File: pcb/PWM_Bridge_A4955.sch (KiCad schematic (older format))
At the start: 18 parts, among them Q3 IPD220N06L3, Q4 IPD220N06L3, Q5 IPD220N06L3, Q6 IPD220N06L3, U5 A4955GLPTR-T

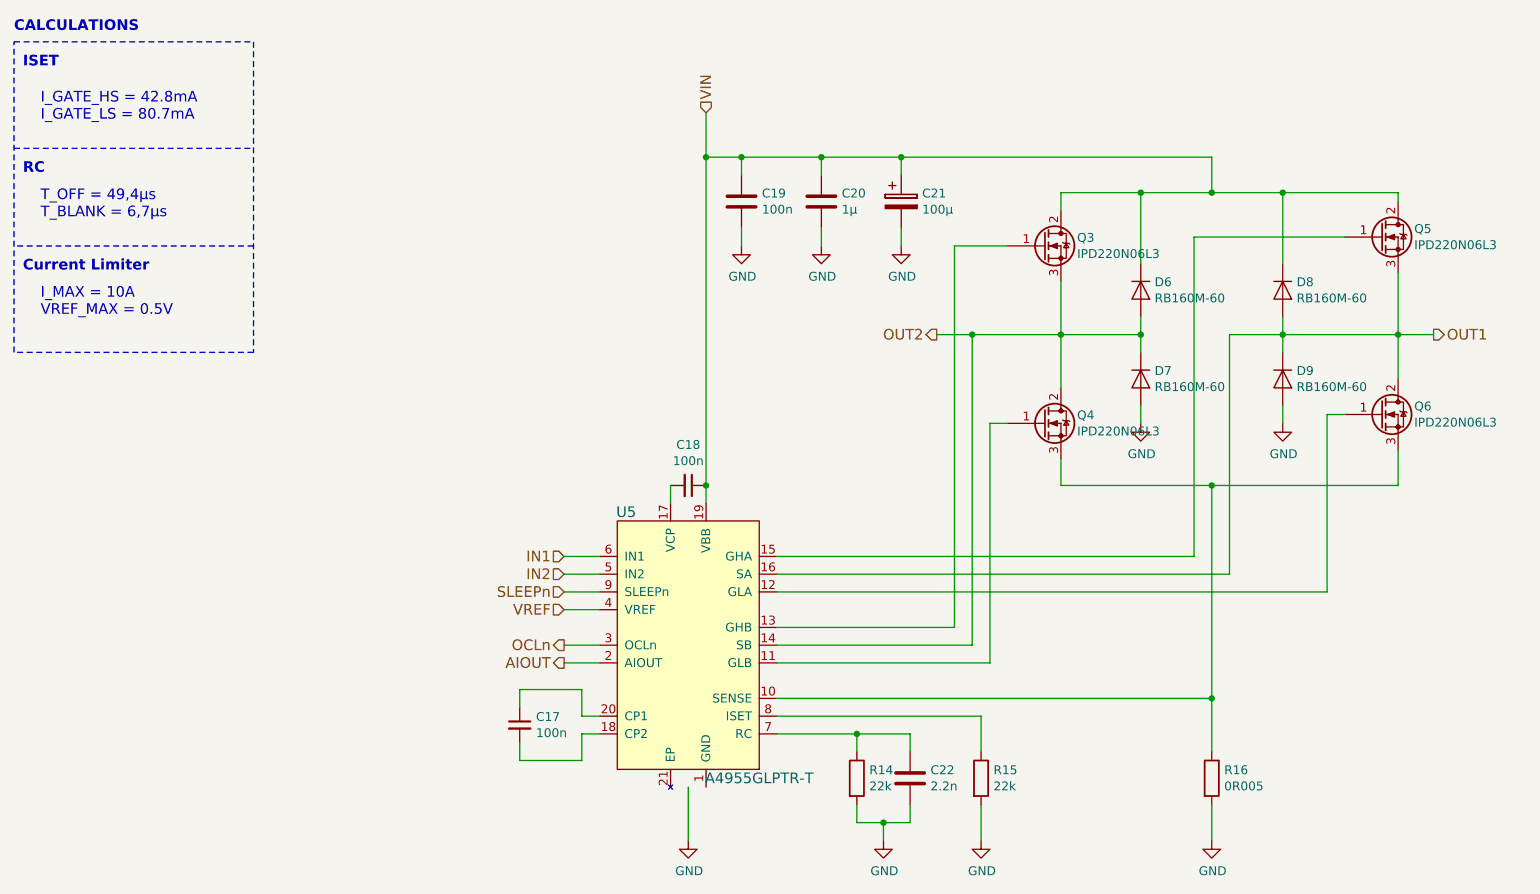
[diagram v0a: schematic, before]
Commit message: Use new library symbols
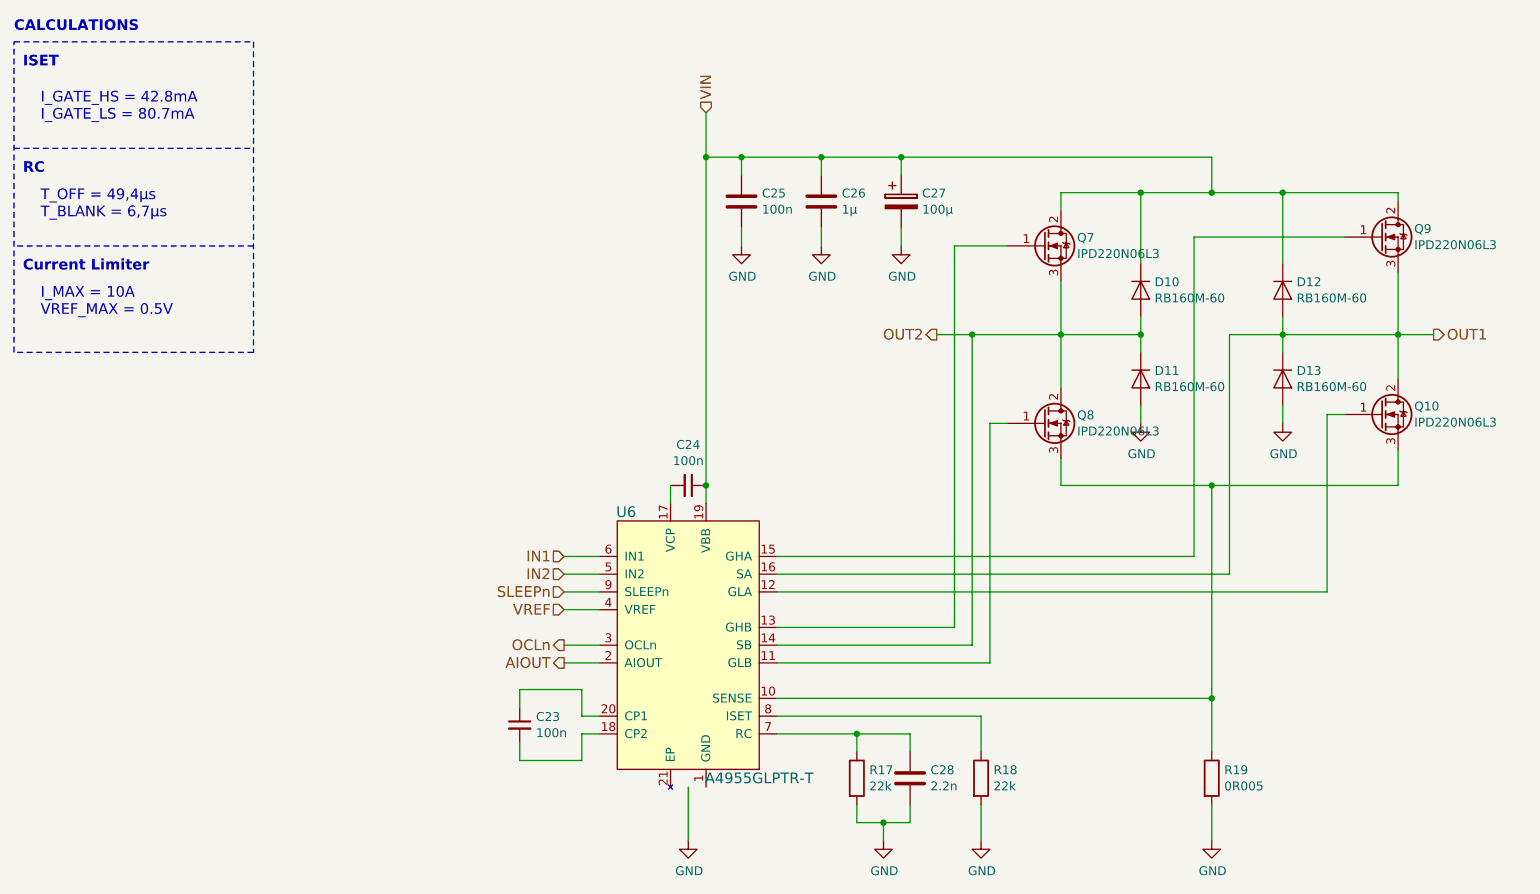
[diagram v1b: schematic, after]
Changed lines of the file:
@@
 $Descr A4 11693 8268
 encoding utf-8
-Sheet 3 7
+Sheet 4 7
 Title "A4955 PWM Bridge"
 Date "2016-10-22"
@@
 AR Path="/58077727/58077F1C" Ref="U5"  Part="1"
 AR Path="/58084D17/58077F1C" Ref="U6"  Part="1"
-F 0 "U5" H 4300 5150 60  0000 C CNN
+F 0 "U6" H 4300 5150 60  0000 C CNN
 F 1 "A4955GLPTR-T" H 5050 3650 60  0000 C CNN
 F 2 "Housings_SSOP:TSSOP-20_4.4x6.5mm_Pitch0.65mm" H 4650 4400 60  0001 C CNN
@@
 AR Path="/58077727/5807829A" Ref="C18"  Part="1"
 AR Path="/58084D17/5807829A" Ref="C24"  Part="1"
-F 0 "C18" V 4421 3500 50  0000 C CNN
+F 0 "C24" V 4421 3500 50  0000 C CNN
 F 1 "100n" V 4512 3500 50  0000 C CNN
 F 2 "Capacitors_SMD:C_0603" H 4650 3500 50  0001 C CNN
@@
 AR Path="/58077727/58078520" Ref="R14"  Part="1"
 AR Path="/58084D17/58078520" Ref="R17"  Part="1"
-F 0 "R14" H 5670 5196 50  0000 L CNN
+F 0 "R17" H 5670 5196 50  0000 L CNN
 F 1 "22k" H 5670 5105 50  0000 L CNN
 F 2 "Resistors_SMD:R_0603" V 5530 5150 50  0001 C CNN
@@
 AR Path="/58077727/5807867B" Ref="C22"  Part="1"
 AR Path="/58084D17/5807867B" Ref="C28"  Part="1"
-F 0 "C22" H 6015 5196 50  0000 L CNN
+F 0 "C28" H 6015 5196 50  0000 L CNN
 F 1 "2.2n" H 6015 5105 50  0000 L CNN
 F 2 "Capacitors_SMD:C_0603" H 5938 5000 50  0001 C CNN
@@
 AR Path="/58077727/580789CE" Ref="R16"  Part="1"
 AR Path="/58084D17/580789CE" Ref="R19"  Part="1"
-F 0 "R16" H 7670 5196 50  0000 L CNN
+F 0 "R19" H 7670 5196 50  0000 L CNN
 F 1 "0R005" H 7670 5105 50  0000 L CNN
 F 2 "Resistors_SMD:R_2512" V 7530 5150 50  0001 C CNN
@@
 AR Path="/58077727/58078C46" Ref="Q3"  Part="1"
 AR Path="/58084D17/58078C46" Ref="Q7"  Part="1"
-F 0 "Q3" H 6841 2196 50  0000 L CNN
+F 0 "Q7" H 6841 2196 50  0000 L CNN
 F 1 "IPD220N06L3" H 6841 2105 50  0000 L CNN
 F 2 "TO_SOT_Packages_SMD:TO-252-2Lead" H 6850 2250 50  0001 C CNN
@@
 AR Path="/58077727/58078E80" Ref="Q5"  Part="1"
 AR Path="/58084D17/58078E80" Ref="Q9"  Part="1"
-F 0 "Q5" H 8741 2146 50  0000 L CNN
+F 0 "Q9" H 8741 2146 50  0000 L CNN
 F 1 "IPD220N06L3" H 8741 2055 50  0000 L CNN
 F 2 "TO_SOT_Packages_SMD:TO-252-2Lead" H 8750 2200 50  0001 C CNN
@@
 AR Path="/58077727/58078ED9" Ref="Q6"  Part="1"
 AR Path="/58084D17/58078ED9" Ref="Q10"  Part="1"
-F 0 "Q6" H 8741 3146 50  0000 L CNN
+F 0 "Q10" H 8741 3146 50  0000 L CNN
 F 1 "IPD220N06L3" H 8741 3055 50  0000 L CNN
 F 2 "TO_SOT_Packages_SMD:TO-252-2Lead" H 8750 3200 50  0001 C CNN
@@
 AR Path="/58077727/58078F3F" Ref="Q4"  Part="1"
 AR Path="/58084D17/58078F3F" Ref="Q8"  Part="1"
-F 0 "Q4" H 6841 3196 50  0000 L CNN
+F 0 "Q8" H 6841 3196 50  0000 L CNN
 F 1 "IPD220N06L3" H 6841 3105 50  0000 L CNN
 F 2 "TO_SOT_Packages_SMD:TO-252-2Lead" H 6850 3250 50  0001 C CNN
@@
 AR Path="/58077727/5807A394" Ref="C19"  Part="1"
 AR Path="/58084D17/5807A394" Ref="C25"  Part="1"
-F 0 "C19" H 5065 1946 50  0000 L CNN
+F 0 "C25" H 5065 1946 50  0000 L CNN
 F 1 "100n" H 5065 1855 50  0000 L CNN
 F 2 "Capacitors_SMD:C_0603" H 4988 1750 50  0001 C CNN
@@
 AR Path="/58077727/5807A62E" Ref="C21"  Part="1"
 AR Path="/58084D17/5807A62E" Ref="C27"  Part="1"
-F 0 "C21" H 5968 1946 50  0000 L CNN
+F 0 "C27" H 5968 1946 50  0000 L CNN
 F 1 "100µ" H 5968 1855 50  0000 L CNN
 F 2 "Capacitors_SMD:c_elec_10x10" H 5888 1750 50  0001 C CNN
@@
 AR Path="/58077727/5807BEA4" Ref="C17"  Part="1"
 AR Path="/58084D17/5807BEA4" Ref="C23"  Part="1"
-F 0 "C17" H 3792 4896 50  0000 L CNN
+F 0 "C23" H 3792 4896 50  0000 L CNN
 F 1 "100n" H 3792 4805 50  0000 L CNN
 F 2 "Capacitors_SMD:C_0603" H 3700 4850 50  0001 C CNN
@@
 AR Path="/58077727/5809AC71" Ref="C20"  Part="1"
 AR Path="/58084D17/5809AC71" Ref="C26"  Part="1"
-F 0 "C20" H 5515 1946 50  0000 L CNN
+F 0 "C26" H 5515 1946 50  0000 L CNN
 F 1 "1µ" H 5515 1855 50  0000 L CNN
 F 2 "Capacitors_SMD:C_0603" H 5438 1750 50  0001 C CNN
@@
 AR Path="/58077727/580A461C" Ref="R15"  Part="1"
 AR Path="/58084D17/580A461C" Ref="R18"  Part="1"
-F 0 "R15" H 6370 5196 50  0000 L CNN
+F 0 "R18" H 6370 5196 50  0000 L CNN
 F 1 "22k" H 6370 5105 50  0000 L CNN
 F 2 "Resistors_SMD:R_0603" V 6230 5150 50  0001 C CNN
@@
 AR Path="/58077727/58151ECD" Ref="D6"  Part="1"
 AR Path="/58084D17/58151ECD" Ref="D10"  Part="1"
-F 0 "D6" V 7154 2478 50  0000 L CNN
+F 0 "D10" V 7154 2478 50  0000 L CNN
 F 1 "RB160M-60" V 7245 2478 50  0000 L CNN
 F 2 "Diodes_SMD:SOD-123" V 7291 2478 50  0001 L CNN
@@
 AR Path="/58077727/581537FD" Ref="D7"  Part="1"
 AR Path="/58084D17/581537FD" Ref="D11"  Part="1"
-F 0 "D7" V 7154 2978 50  0000 L CNN
+F 0 "D11" V 7154 2978 50  0000 L CNN
 F 1 "RB160M-60" V 7245 2978 50  0000 L CNN
 F 2 "Diodes_SMD:SOD-123" V 7291 2978 50  0001 L CNN
@@
 AR Path="/58077727/58153EBB" Ref="D9"  Part="1"
 AR Path="/58084D17/58153EBB" Ref="D13"  Part="1"
-F 0 "D9" V 7954 2978 50  0000 L CNN
+F 0 "D13" V 7954 2978 50  0000 L CNN
 F 1 "RB160M-60" V 8045 2978 50  0000 L CNN
 F 2 "Diodes_SMD:SOD-123" V 8091 2978 50  0001 L CNN
@@
 AR Path="/58077727/58153F12" Ref="D8"  Part="1"
 AR Path="/58084D17/58153F12" Ref="D12"  Part="1"
-F 0 "D8" V 7954 2478 50  0000 L CNN
+F 0 "D12" V 7954 2478 50  0000 L CNN
 F 1 "RB160M-60" V 8045 2478 50  0000 L CNN
 F 2 "Diodes_SMD:SOD-123" V 8091 2478 50  0001 L CNN

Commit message: Improve pcb routing
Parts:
- U5: footprint Housings_SSOP:TSSOP-20_4.4x6.5mm_Pitch0.65mm -> Housings_SSOP:ETSSOP-20-1EP_4.4x6.5mm_Pitch0.65mm
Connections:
- net GND: now also U5.1 (GND), U5.21 (EP)
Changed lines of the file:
@@
 $Descr A4 11693 8268
 encoding utf-8
-Sheet 4 7
+Sheet 3 7
 Title "A4955 PWM Bridge"
 Date "2016-10-22"
@@
 AR Path="/58077727/58077F1C" Ref="U5"  Part="1"
 AR Path="/58084D17/58077F1C" Ref="U6"  Part="1"
-F 0 "U6" H 4300 5150 60  0000 C CNN
-F 1 "A4955GLPTR-T" H 5050 3650 60  0000 C CNN
-F 2 "Housings_SSOP:TSSOP-20_4.4x6.5mm_Pitch0.65mm" H 4650 4400 60  0001 C CNN
+F 0 "U5" H 4300 5150 60  0000 C CNN
+F 1 "A4955GLPTR-T" H 5100 3650 60  0000 C CNN
+F 2 "Housings_SSOP:ETSSOP-20-1EP_4.4x6.5mm_Pitch0.65mm" H 4650 4400 60  0001 C CNN
 F 3 "http://www.allegromicro.com/~/media/Files/Datasheets/A4955-Datasheet.ashx?la=en" H 4650 4400 60  0001 C CNN
 F 4 "620-1770-1-ND" H 4650 4400 60  0001 C CNN "Digi-Key Part Number"
@@
 AR Path="/58077727/5807829A" Ref="C18"  Part="1"
 AR Path="/58084D17/5807829A" Ref="C24"  Part="1"
-F 0 "C24" V 4421 3500 50  0000 C CNN
+F 0 "C18" V 4421 3500 50  0000 C CNN
 F 1 "100n" V 4512 3500 50  0000 C CNN
 F 2 "Capacitors_SMD:C_0603" H 4650 3500 50  0001 C CNN
@@
 AR Path="/58077727/58078520" Ref="R14"  Part="1"
 AR Path="/58084D17/58078520" Ref="R17"  Part="1"
-F 0 "R17" H 5670 5196 50  0000 L CNN
+F 0 "R14" H 5670 5196 50  0000 L CNN
 F 1 "22k" H 5670 5105 50  0000 L CNN
 F 2 "Resistors_SMD:R_0603" V 5530 5150 50  0001 C CNN
@@
 AR Path="/58077727/5807867B" Ref="C22"  Part="1"
 AR Path="/58084D17/5807867B" Ref="C28"  Part="1"
-F 0 "C28" H 6015 5196 50  0000 L CNN
+F 0 "C22" H 6015 5196 50  0000 L CNN
 F 1 "2.2n" H 6015 5105 50  0000 L CNN
 F 2 "Capacitors_SMD:C_0603" H 5938 5000 50  0001 C CNN
@@
 AR Path="/58077727/580787DB" Ref="#PWR063"  Part="1"
 AR Path="/58084D17/580787DB" Ref="#PWR072"  Part="1"
-F 0 "#PWR072" H 5750 5250 50  0001 C CNN
+F 0 "#PWR063" H 5750 5250 50  0001 C CNN
 F 1 "GND" H 5755 5327 50  0000 C CNN
 F 2 "" H 5750 5500 50  0000 C CNN
@@
 L GND #PWR064
 U 1 1 58078835
-P 4650 5500
+P 4750 5500
 AR Path="/58077727/58078835" Ref="#PWR064"  Part="1"
 AR Path="/58084D17/58078835" Ref="#PWR073"  Part="1"
-F 0 "#PWR073" H 4650 5250 50  0001 C CNN
-F 1 "GND" H 4655 5327 50  0000 C CNN
-F 2 "" H 4650 5500 50  0000 C CNN
-F 3 "" H 4650 5500 50  0000 C CNN
-	1    4650 5500
+F 0 "#PWR064" H 4750 5250 50  0001 C CNN
+F 1 "GND" H 4755 5327 50  0000 C CNN
+F 2 "" H 4750 5500 50  0000 C CNN
+F 3 "" H 4750 5500 50  0000 C CNN
+	1    4750 5500
 	1    0    0    -1
 $EndComp
@@
 AR Path="/58077727/580789CE" Ref="R16"  Part="1"
 AR Path="/58084D17/580789CE" Ref="R19"  Part="1"
-F 0 "R19" H 7670 5196 50  0000 L CNN
+F 0 "R16" H 7670 5196 50  0000 L CNN
 F 1 "0R005" H 7670 5105 50  0000 L CNN
 F 2 "Resistors_SMD:R_2512" V 7530 5150 50  0001 C CNN
@@
 AR Path="/58077727/58078AB1" Ref="#PWR065"  Part="1"
 AR Path="/58084D17/58078AB1" Ref="#PWR074"  Part="1"
-F 0 "#PWR074" H 7600 5250 50  0001 C CNN
+F 0 "#PWR065" H 7600 5250 50  0001 C CNN
 F 1 "GND" H 7605 5327 50  0000 C CNN
 F 2 "" H 7600 5500 50  0000 C CNN
@@
 AR Path="/58077727/58078C46" Ref="Q3"  Part="1"
 AR Path="/58084D17/58078C46" Ref="Q7"  Part="1"
-F 0 "Q7" H 6841 2196 50  0000 L CNN
+F 0 "Q3" H 6841 2196 50  0000 L CNN
 F 1 "IPD220N06L3" H 6841 2105 50  0000 L CNN
 F 2 "TO_SOT_Packages_SMD:TO-252-2Lead" H 6850 2250 50  0001 C CNN
@@
 AR Path="/58077727/58078E80" Ref="Q5"  Part="1"
 AR Path="/58084D17/58078E80" Ref="Q9"  Part="1"
-F 0 "Q9" H 8741 2146 50  0000 L CNN
+F 0 "Q5" H 8741 2146 50  0000 L CNN
 F 1 "IPD220N06L3" H 8741 2055 50  0000 L CNN
 F 2 "TO_SOT_Packages_SMD:TO-252-2Lead" H 8750 2200 50  0001 C CNN
@@
 AR Path="/58077727/58078ED9" Ref="Q6"  Part="1"
 AR Path="/58084D17/58078ED9" Ref="Q10"  Part="1"
-F 0 "Q10" H 8741 3146 50  0000 L CNN
+F 0 "Q6" H 8741 3146 50  0000 L CNN
 F 1 "IPD220N06L3" H 8741 3055 50  0000 L CNN
 F 2 "TO_SOT_Packages_SMD:TO-252-2Lead" H 8750 3200 50  0001 C CNN
@@
 AR Path="/58077727/58078F3F" Ref="Q4"  Part="1"
 AR Path="/58084D17/58078F3F" Ref="Q8"  Part="1"
-F 0 "Q8" H 6841 3196 50  0000 L CNN
+F 0 "Q4" H 6841 3196 50  0000 L CNN
 F 1 "IPD220N06L3" H 6841 3105 50  0000 L CNN
 F 2 "TO_SOT_Packages_SMD:TO-252-2Lead" H 6850 3250 50  0001 C CNN
@@
 AR Path="/58077727/5807A394" Ref="C19"  Part="1"
 AR Path="/58084D17/5807A394" Ref="C25"  Part="1"
-F 0 "C25" H 5065 1946 50  0000 L CNN
+F 0 "C19" H 5065 1946 50  0000 L CNN
 F 1 "100n" H 5065 1855 50  0000 L CNN
 F 2 "Capacitors_SMD:C_0603" H 4988 1750 50  0001 C CNN
@@
 AR Path="/58077727/5807A4C6" Ref="#PWR066"  Part="1"
 AR Path="/58084D17/5807A4C6" Ref="#PWR075"  Part="1"
-F 0 "#PWR075" H 4950 1900 50  0001 C CNN
+F 0 "#PWR066" H 4950 1900 50  0001 C CNN
 F 1 "GND" H 4955 1977 50  0000 C CNN
 F 2 "" H 4950 2150 50  0000 C CNN
@@
 AR Path="/58077727/5807A62E" Ref="C21"  Part="1"
 AR Path="/58084D17/5807A62E" Ref="C27"  Part="1"
-F 0 "C27" H 5968 1946 50  0000 L CNN
+F 0 "C21" H 5968 1946 50  0000 L CNN
 F 1 "100µ" H 5968 1855 50  0000 L CNN
 F 2 "Capacitors_SMD:c_elec_10x10" H 5888 1750 50  0001 C CNN
@@
 AR Path="/58077727/5807A964" Ref="#PWR067"  Part="1"
 AR Path="/58084D17/5807A964" Ref="#PWR076"  Part="1"
-F 0 "#PWR076" H 5850 1900 50  0001 C CNN
+F 0 "#PWR067" H 5850 1900 50  0001 C CNN
 F 1 "GND" H 5855 1977 50  0000 C CNN
 F 2 "" H 5850 2150 50  0000 C CNN
@@
 AR Path="/58077727/5807BEA4" Ref="C17"  Part="1"
 AR Path="/58084D17/5807BEA4" Ref="C23"  Part="1"
-F 0 "C23" H 3792 4896 50  0000 L CNN
+F 0 "C17" H 3792 4896 50  0000 L CNN
 F 1 "100n" H 3792 4805 50  0000 L CNN
 F 2 "Capacitors_SMD:C_0603" H 3700 4850 50  0001 C CNN
@@
 AR Path="/58077727/5809AC71" Ref="C20"  Part="1"
 AR Path="/58084D17/5809AC71" Ref="C26"  Part="1"
-F 0 "C26" H 5515 1946 50  0000 L CNN
+F 0 "C20" H 5515 1946 50  0000 L CNN
 F 1 "1µ" H 5515 1855 50  0000 L CNN
 F 2 "Capacitors_SMD:C_0603" H 5438 1750 50  0001 C CNN
@@
 AR Path="/58084D17/5809ACB6" Ref="#PWR077"  Part="1"
 AR Path="/58077727/5809ACB6" Ref="#PWR068"  Part="1"
-F 0 "#PWR077" H 5400 1900 50  0001 C CNN
+F 0 "#PWR068" H 5400 1900 50  0001 C CNN
 F 1 "GND" H 5405 1977 50  0000 C CNN
 F 2 "" H 5400 2150 50  0000 C CNN
@@
 AR Path="/58077727/580A461C" Ref="R15"  Part="1"
 AR Path="/58084D17/580A461C" Ref="R18"  Part="1"
-F 0 "R18" H 6370 5196 50  0000 L CNN
+F 0 "R15" H 6370 5196 50  0000 L CNN
 F 1 "22k" H 6370 5105 50  0000 L CNN
 F 2 "Resistors_SMD:R_0603" V 6230 5150 50  0001 C CNN
@@
 AR Path="/58077727/580A46B3" Ref="#PWR069"  Part="1"
 AR Path="/58084D17/580A46B3" Ref="#PWR078"  Part="1"
-F 0 "#PWR078" H 6300 5250 50  0001 C CNN
+F 0 "#PWR069" H 6300 5250 50  0001 C CNN
 F 1 "GND" H 6305 5327 50  0000 C CNN
 F 2 "" H 6300 5500 50  0000 C CNN
@@
 AR Path="/58077727/58151ECD" Ref="D6"  Part="1"
 AR Path="/58084D17/58151ECD" Ref="D10"  Part="1"
-F 0 "D10" V 7154 2478 50  0000 L CNN
+F 0 "D6" V 7154 2478 50  0000 L CNN
 F 1 "RB160M-60" V 7245 2478 50  0000 L CNN
 F 2 "Diodes_SMD:SOD-123" V 7291 2478 50  0001 L CNN
@@
 AR Path="/58077727/581537FD" Ref="D7"  Part="1"
 AR Path="/58084D17/581537FD" Ref="D11"  Part="1"
-F 0 "D11" V 7154 2978 50  0000 L CNN
+F 0 "D7" V 7154 2978 50  0000 L CNN
 F 1 "RB160M-60" V 7245 2978 50  0000 L CNN
 F 2 "Diodes_SMD:SOD-123" V 7291 2978 50  0001 L CNN
@@
 AR Path="/58077727/58153EBB" Ref="D9"  Part="1"
 AR Path="/58084D17/58153EBB" Ref="D13"  Part="1"
-F 0 "D13" V 7954 2978 50  0000 L CNN
+F 0 "D9" V 7954 2978 50  0000 L CNN
 F 1 "RB160M-60" V 8045 2978 50  0000 L CNN
 F 2 "Diodes_SMD:SOD-123" V 8091 2978 50  0001 L CNN
@@
 AR Path="/58077727/58153F12" Ref="D8"  Part="1"
 AR Path="/58084D17/58153F12" Ref="D12"  Part="1"
-F 0 "D12" V 7954 2478 50  0000 L CNN
+F 0 "D8" V 7954 2478 50  0000 L CNN
 F 1 "RB160M-60" V 8045 2478 50  0000 L CNN
 F 2 "Diodes_SMD:SOD-123" V 8091 2478 50  0001 L CNN
@@
 AR Path="/58077727/581550B7" Ref="#PWR070"  Part="1"
 AR Path="/58084D17/581550B7" Ref="#PWR079"  Part="1"
-F 0 "#PWR079" H 8000 2900 50  0001 C CNN
+F 0 "#PWR070" H 8000 2900 50  0001 C CNN
 F 1 "GND" H 8005 2977 50  0000 C CNN
 F 2 "" H 8000 3150 50  0000 C CNN
@@
 AR Path="/58077727/58155164" Ref="#PWR071"  Part="1"
 AR Path="/58084D17/58155164" Ref="#PWR080"  Part="1"
-F 0 "#PWR080" H 7200 2900 50  0001 C CNN
+F 0 "#PWR071" H 7200 2900 50  0001 C CNN
 F 1 "GND" H 7205 2977 50  0000 C CNN
 F 2 "" H 7200 3150 50  0000 C CNN
@@
 	5600 5400 5600 5300
 Wire Wire Line
-	4650 5200 4650 5500
+	4750 5200 4750 5500
 Wire Wire Line
 	5750 5500 5750 5400
@@
 Wire Notes Line
 	850  2750 850  1000
+$Comp
+L GND #PWR?
+U 1 1 582EE915
+P 4550 5500
+F 0 "#PWR?" H 4550 5250 50  0001 C CNN
+F 1 "GND" H 4555 5327 50  0000 C CNN
+F 2 "" H 4550 5500 50  0000 C CNN
+F 3 "" H 4550 5500 50  0000 C CNN
+	1    4550 5500
+	1    0    0    -1
+$EndComp
+Wire Wire Line
+	4550 5500 4550 5200
 $EndSCHEMATC
